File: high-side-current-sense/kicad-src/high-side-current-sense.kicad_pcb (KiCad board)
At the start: 2 copper layers, 34.3 x 26 mm, 10 parts, among them J1 Conn_01x04, J2 Conn_01x04, U1 MAX4209HAUA

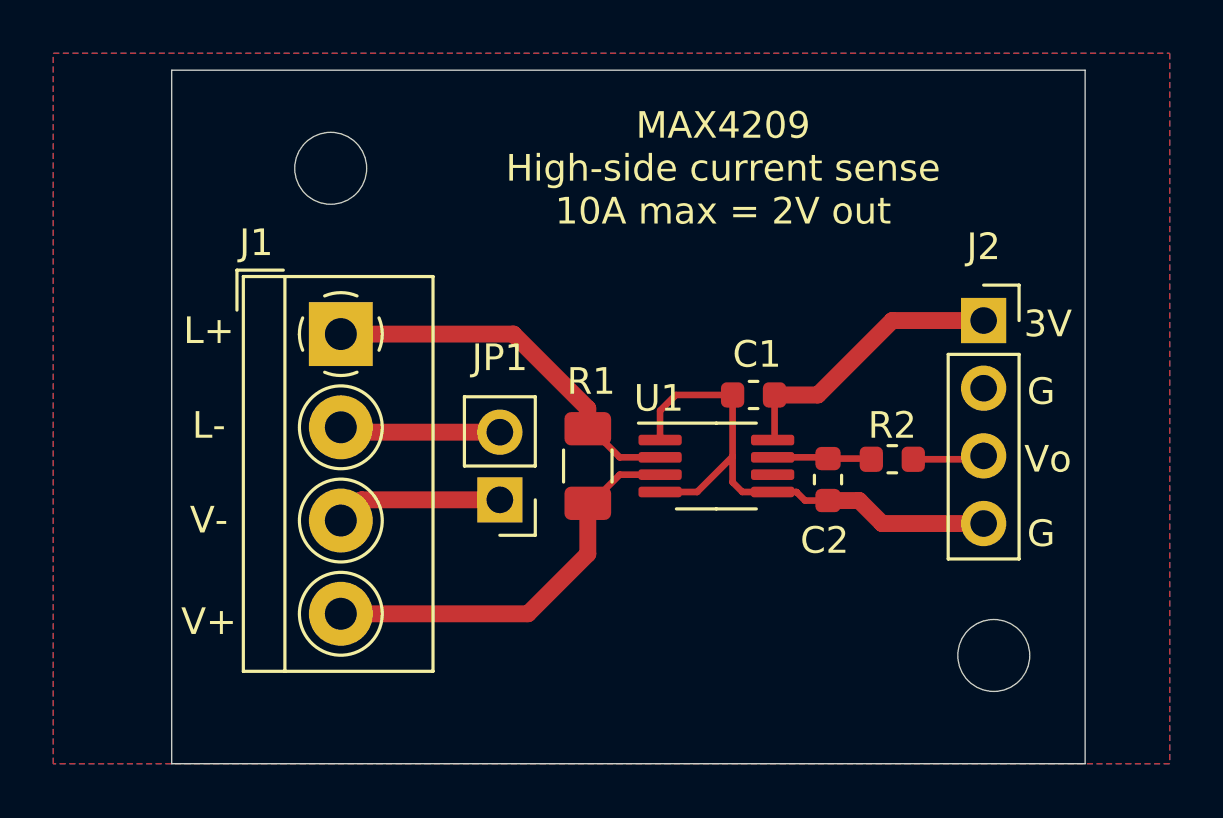
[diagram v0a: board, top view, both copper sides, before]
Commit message: stabilizes output with cap on FB pin
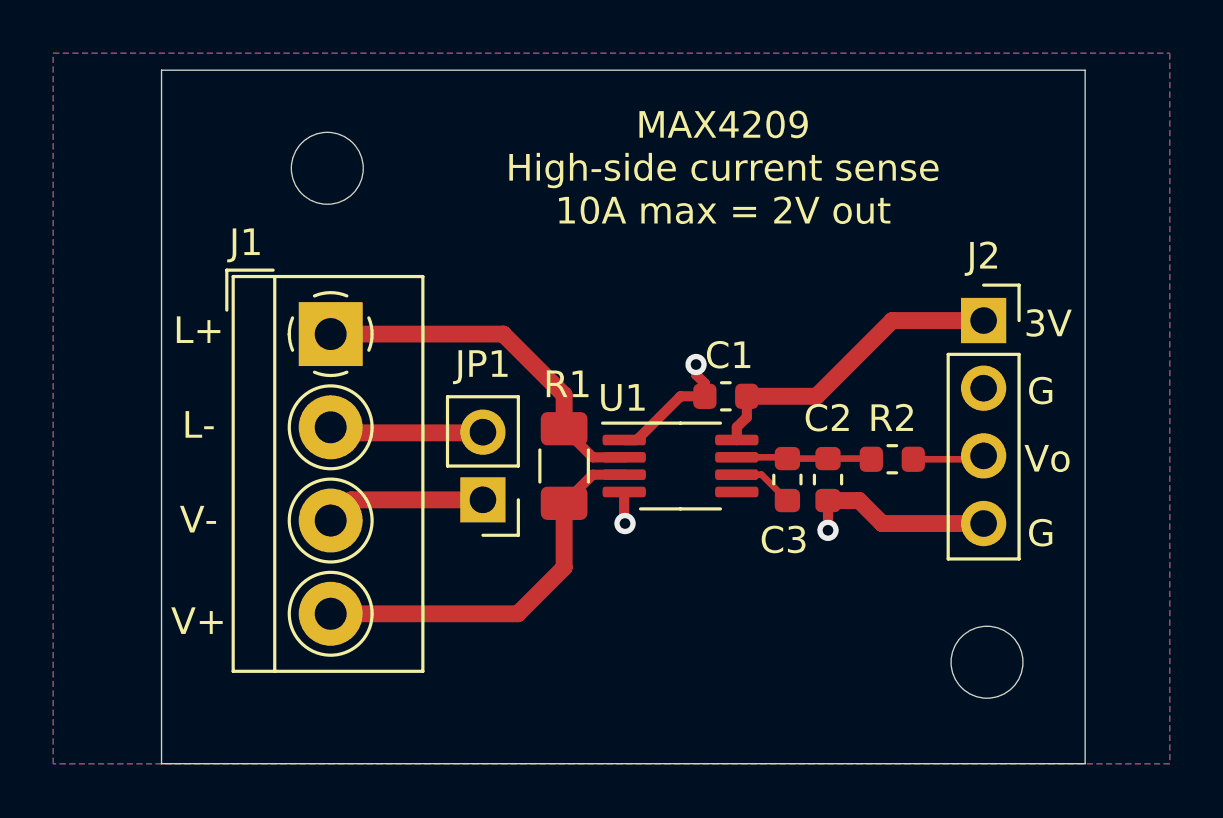
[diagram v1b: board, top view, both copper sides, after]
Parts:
- added C3: 10nF, Capacitor_SMD:C_0603_1608Metric, F.Cu at (163.4, 99.8)
- moved U1 1.35 mm to (159.4, 99.3)
- moved C1 1.04 mm to (161.1, 96.7)
- moved R1 0.89 mm to (155.1, 99.3)
- moved JP1 0.63 mm to (152.0, 100.6)
- moved J1 0.38 mm to (146.3, 94.4)
- moved H2 0.36 mm to (170.9, 106.7)
- moved H1 0.13 mm to (146.2, 88.1)
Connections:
- U1 pad 5: GND -> Net-(U1-Pad5)
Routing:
- net GND: track 20.9 -> 13.8 mm, vias 0 -> 3
- net Net-(C3-Pad1): track 0.00 -> 2.30 mm
- net Net-(C2-Pad1): track 3.73 -> 5.08 mm
- net +3V3: track 11.0 -> 12.1 mm
- net /SUPPLY+: track 15.3 -> 14.6 mm
- net /LOAD+: track 14.3 -> 13.7 mm
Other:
- board size 34.3 x 26 mm -> 34.7 x 26 mm
